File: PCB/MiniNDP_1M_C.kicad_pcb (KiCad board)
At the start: 2 copper layers, 60 x 34 mm, 18 parts, among them J1 Conn_02x20_Odd_Even, U1 AS6C8008_TSOPII, U2 HC238, U3 4040, U4 FCT841

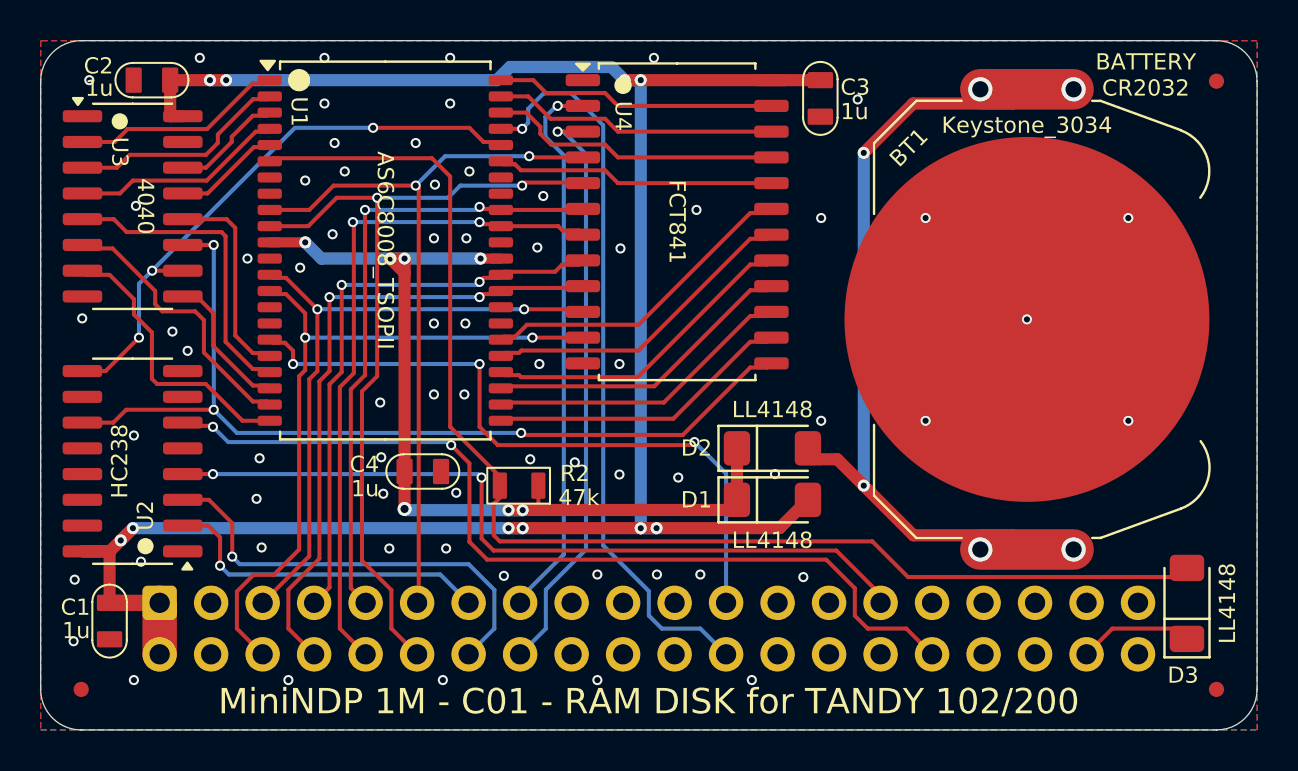
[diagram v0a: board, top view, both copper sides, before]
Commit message: 1M_C pwr & gnd traces
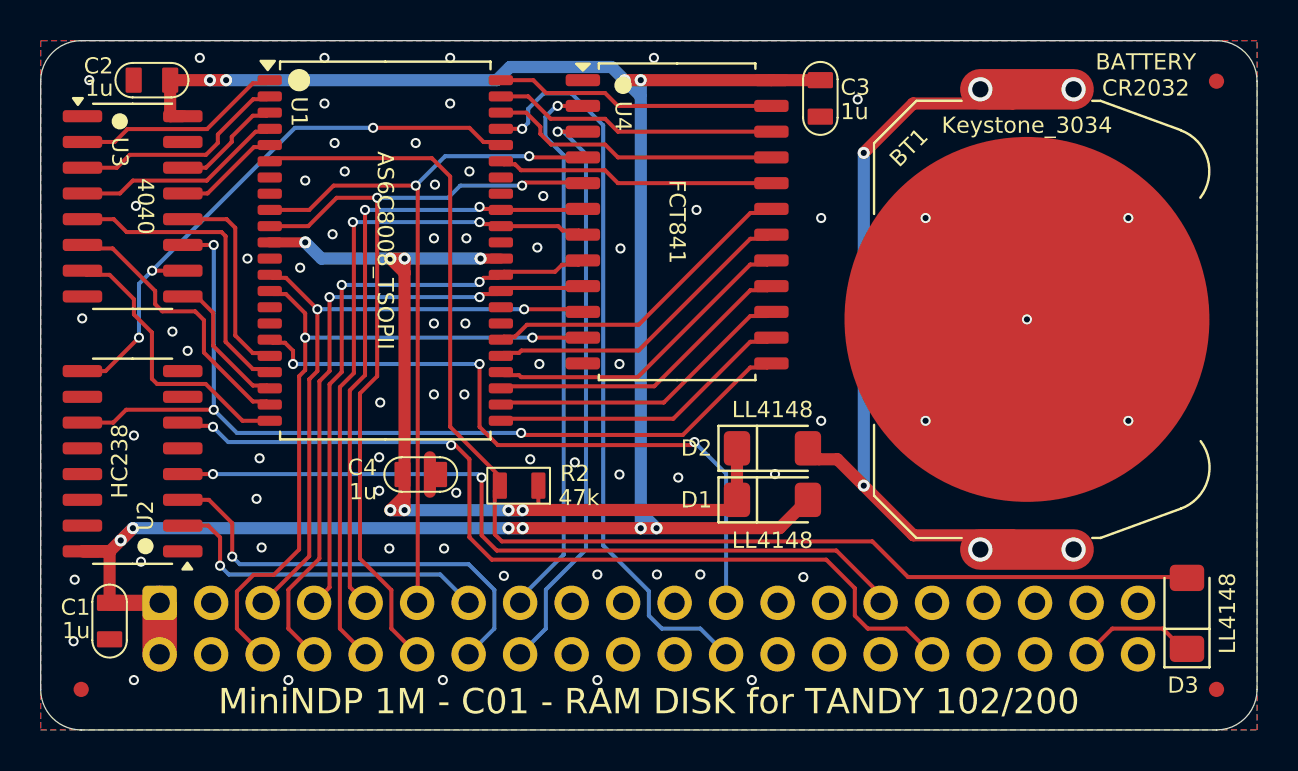
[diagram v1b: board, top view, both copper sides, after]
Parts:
- moved D3 0.49 mm to (178.5, 114.3)
- moved C4 0.18 mm to (140.7, 107.4)
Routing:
- net VMEM: track 47.7 -> 50.1 mm, vias 7 -> 8
- net VBUS: track 107.0 -> 109.2 mm
- net GND: track 0.00 -> 1.70 mm

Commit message: 512_F 1M_C remove ramrst diode, 1u caps
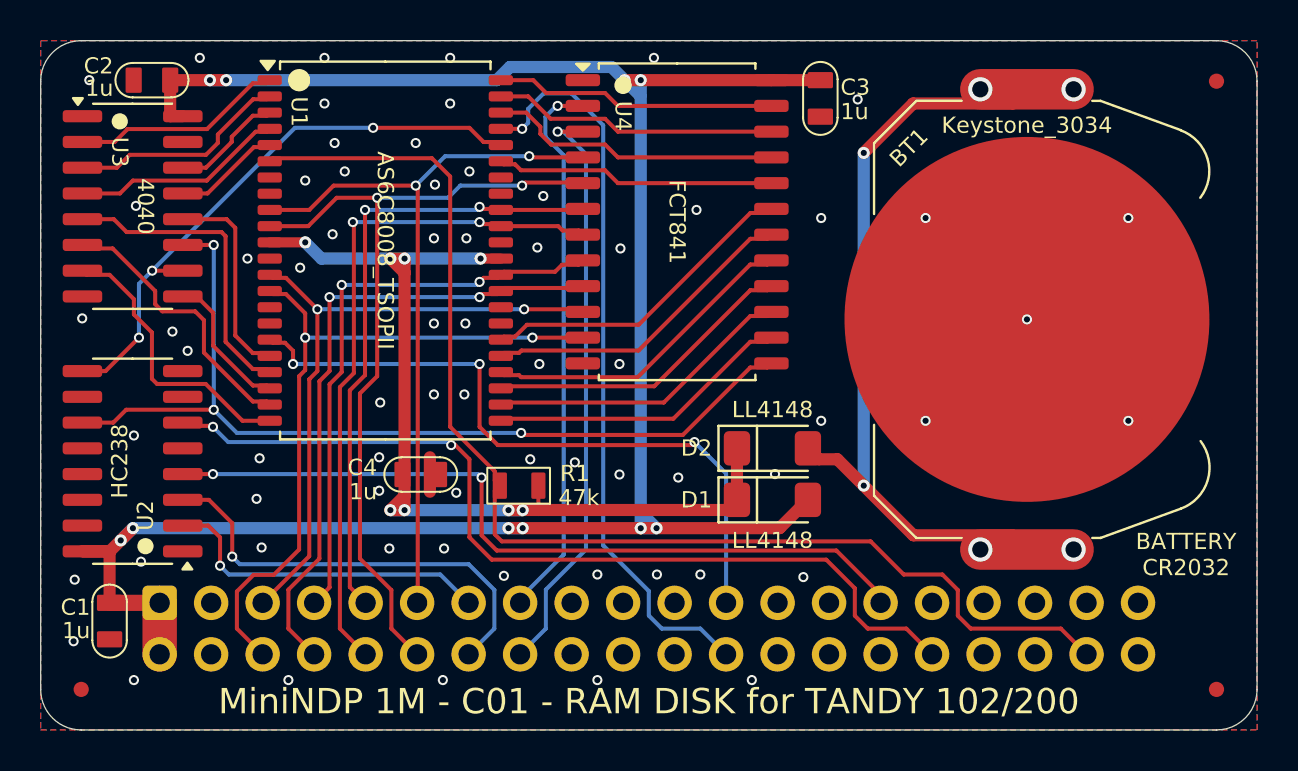
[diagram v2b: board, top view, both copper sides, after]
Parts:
- removed D3: LL4148, 000_LOCAL:D_MiniMELF
- renumbered R2 to R1
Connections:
- R1 pad 2: /SLEEP -> /RAMRST
- U1 pad 6: /SLEEP -> /RAMRST
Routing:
- net /SLEEP: track 63.1 -> 0.00 mm
- net /RAMRST: track 5.89 -> 60.5 mm

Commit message: easy boards add 47u cap, remove ramrst diode
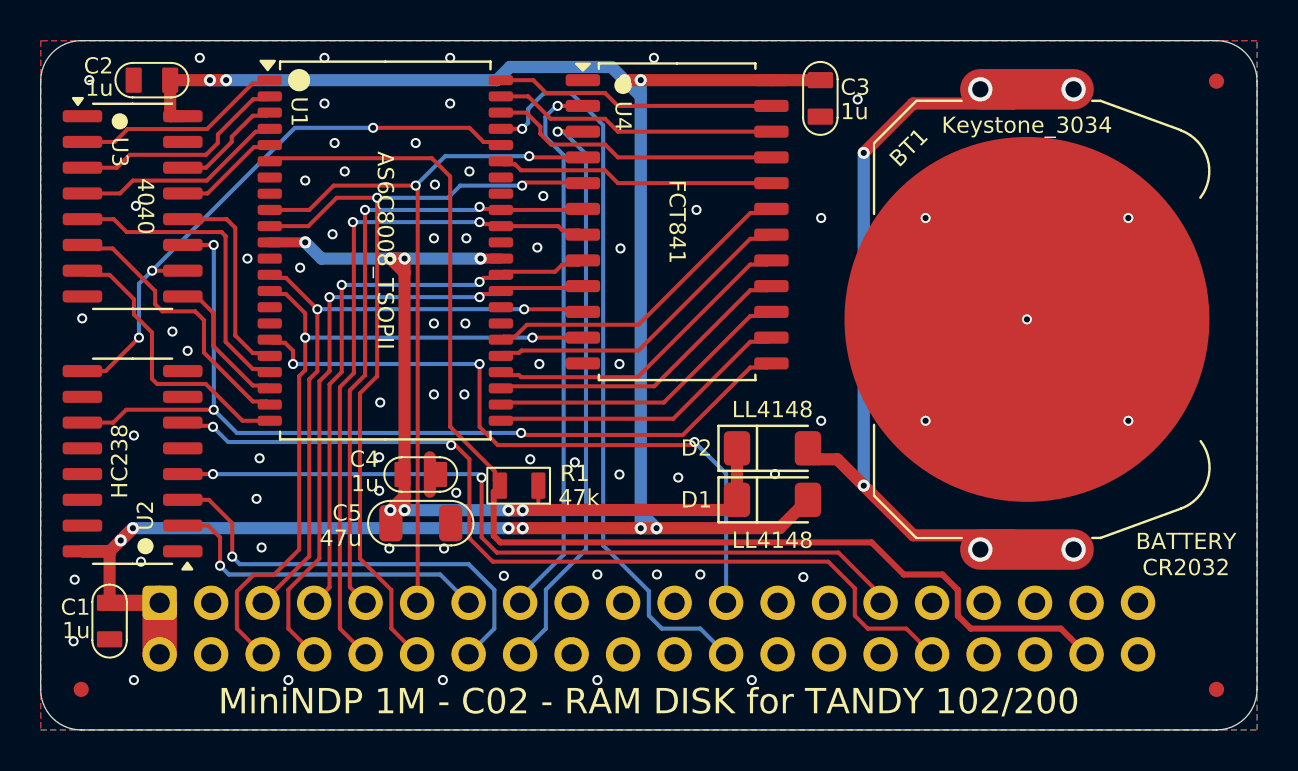
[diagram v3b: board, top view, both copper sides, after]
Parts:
- added C5: 47u, 000_LOCAL:C_1206, F.Cu at (140.7, 109.8)

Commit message: notes in historical, big cap in 1M_C
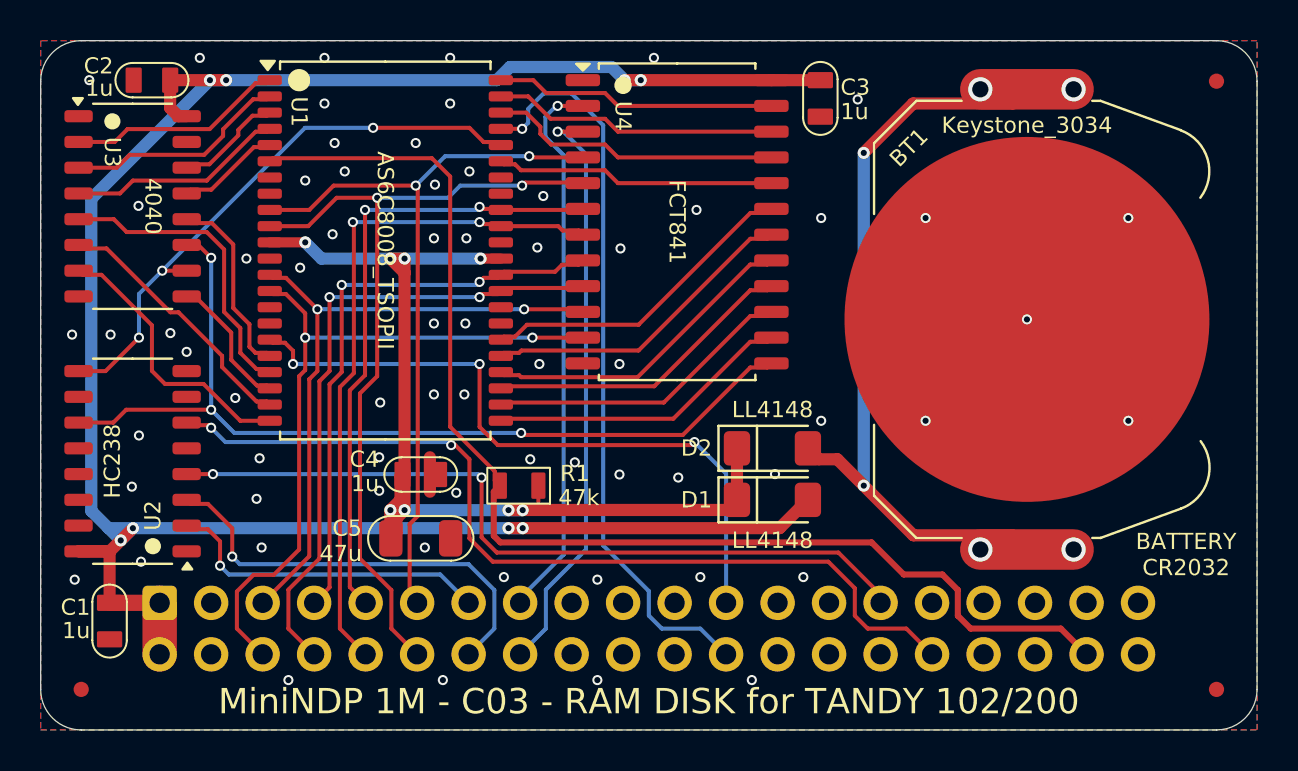
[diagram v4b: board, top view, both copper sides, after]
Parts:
- moved C5 0.75 mm to (140.7, 110.6)
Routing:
- net VMEM: track 50.1 -> 54.3 mm
- net VBUS: track 109.2 -> 111.4 mm, vias 10 -> 8
- net /A8: track 10.2 -> 9.38 mm
- net /A2: track 13.8 -> 13.0 mm
- net GND: vias 68 -> 67
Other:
- board text added: "RAM DISK for TANDY 102/200"
- board text added: "X% : 129=BANK0 133=BANK1 137=BANK2 141=BANK3 N% : 0-255 offset counts 0-1023"
- board text removed: "X% : 129=BANK0 133=BANK1 137=BANK2 141=BANK3 N% : 0-255 offset rolls over to 0 after 1023"

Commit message: bundle code font
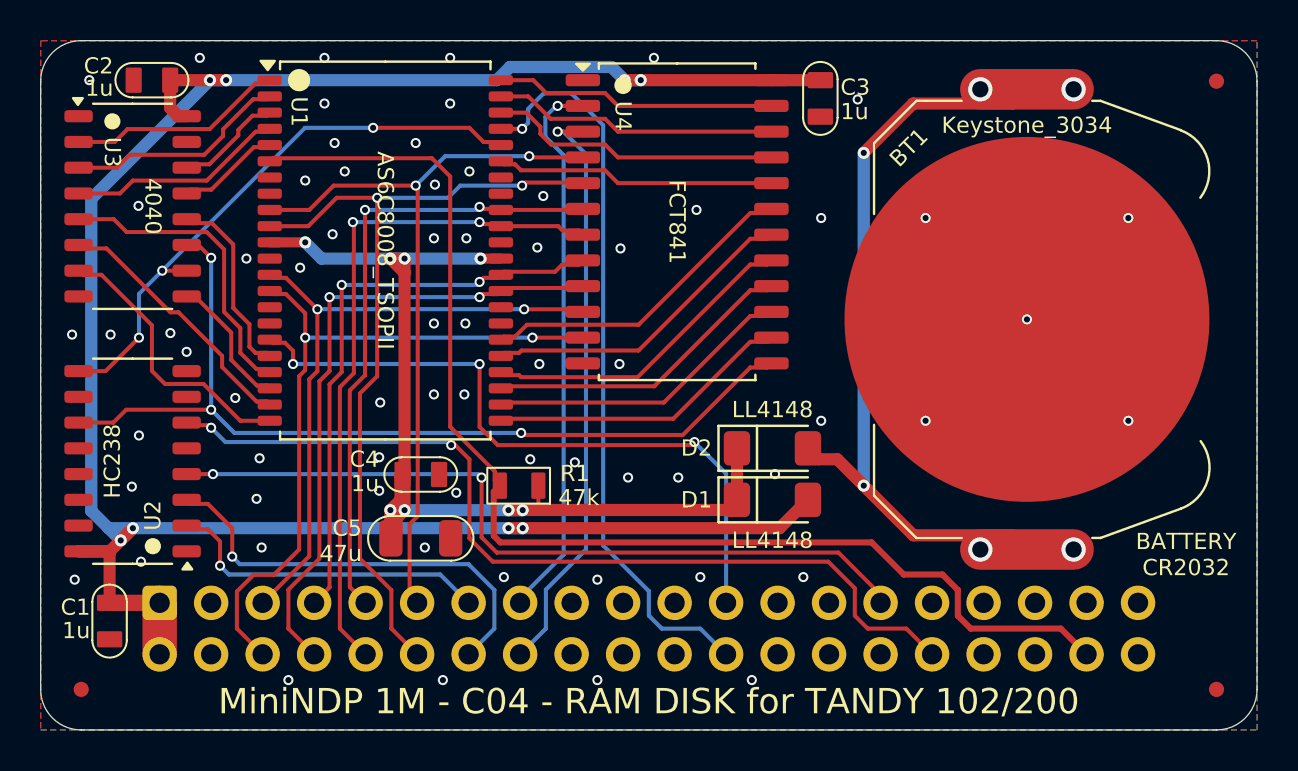
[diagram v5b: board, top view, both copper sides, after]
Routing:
- net GND: track 1.70 -> 0.00 mm

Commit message: 1M_C move passives around
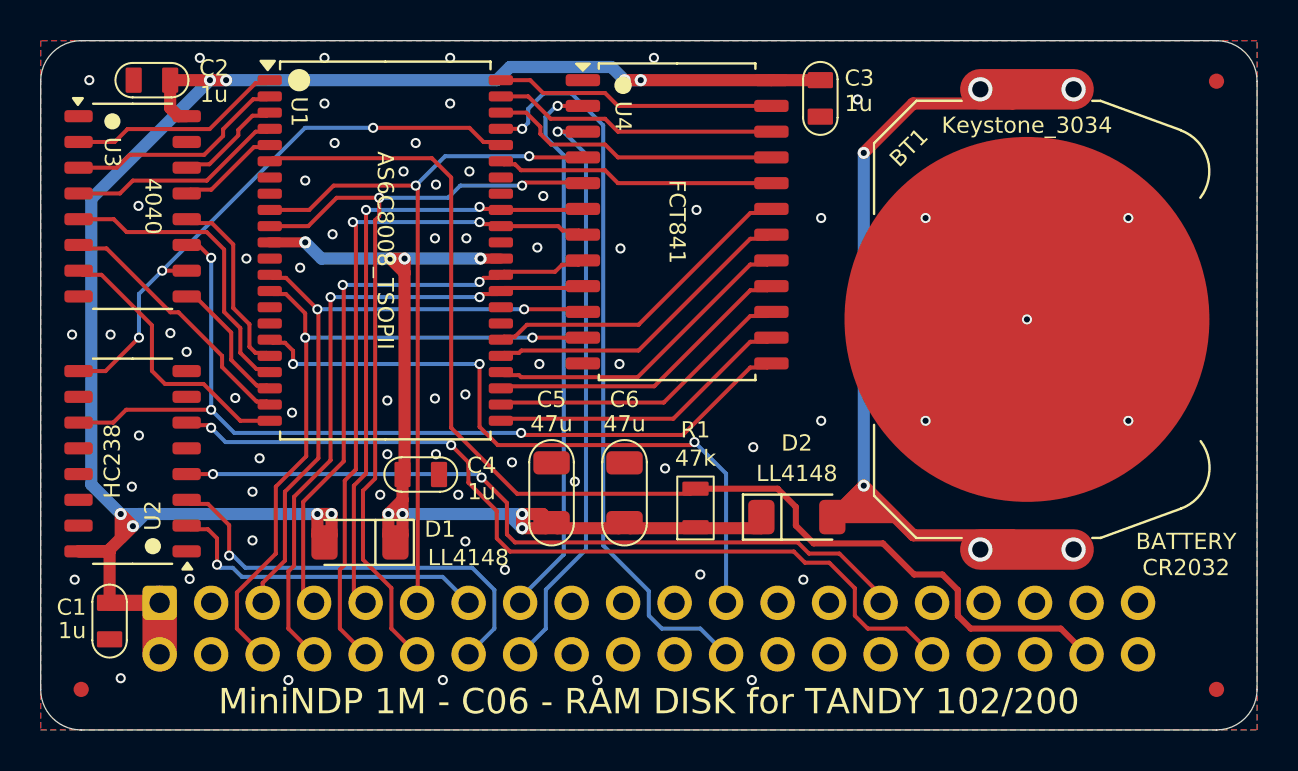
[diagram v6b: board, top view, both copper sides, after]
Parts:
- added C6: 47u, 000_LOCAL:C_1206, F.Cu at (150.8, 108.3)
- moved D1 20.5 mm to (137.7, 110.8), turned to 180 degrees
- moved R1 8.77 mm to (154.2, 109.1), turned to 90 degrees
- moved C5 6.83 mm to (147.2, 108.3), turned to 90 degrees
- moved D2 3.60 mm to (159.2, 109.5)
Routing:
- net VBUS: track 111.4 -> 87.3 mm
- net /RAMRST: track 60.6 -> 59.2 mm
- net +BATT: track 38.6 -> 37.3 mm
- net /(A): track 44.6 -> 43.7 mm
- net /~{Y0}: track 38.8 -> 38.0 mm
- net /AD0: track 35.2 -> 34.7 mm
- net GND: vias 67 -> 66
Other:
- board text added: "Install the font in the font directory for the BASIC code."
- board text added: "Use ENIG copper finish for gold battery terminal."
- board text removed: "Use ENIG copper finish for gold plated battery terminal"

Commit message: 1M_C move passives around
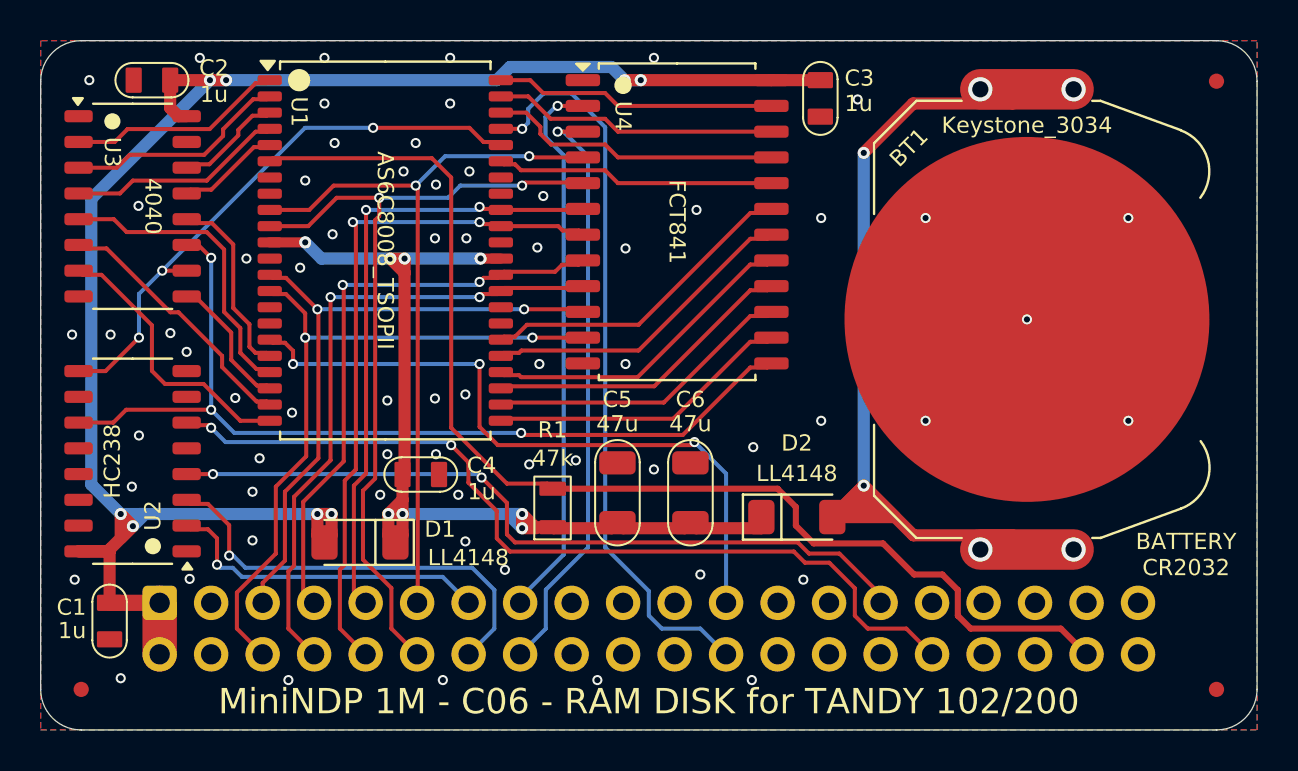
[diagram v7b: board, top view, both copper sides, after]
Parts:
- moved R1 7.05 mm to (147.2, 109.1)
- moved C5 3.25 mm to (150.4, 108.3)
- moved C6 3.25 mm to (154.0, 108.3)
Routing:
- net VMEM: track 54.4 -> 50.4 mm
